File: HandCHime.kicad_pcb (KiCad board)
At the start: 4 copper layers, 38.1 x 22.6 mm, 18 parts, among them J1 USB_C_Receptacle_USB2.0, J2 Pins, SW0 BOOT, SW1 Row 0, Col 0, SW2 Row 0, Col 1, U1 CH552T, U2 USBLC6-2P6

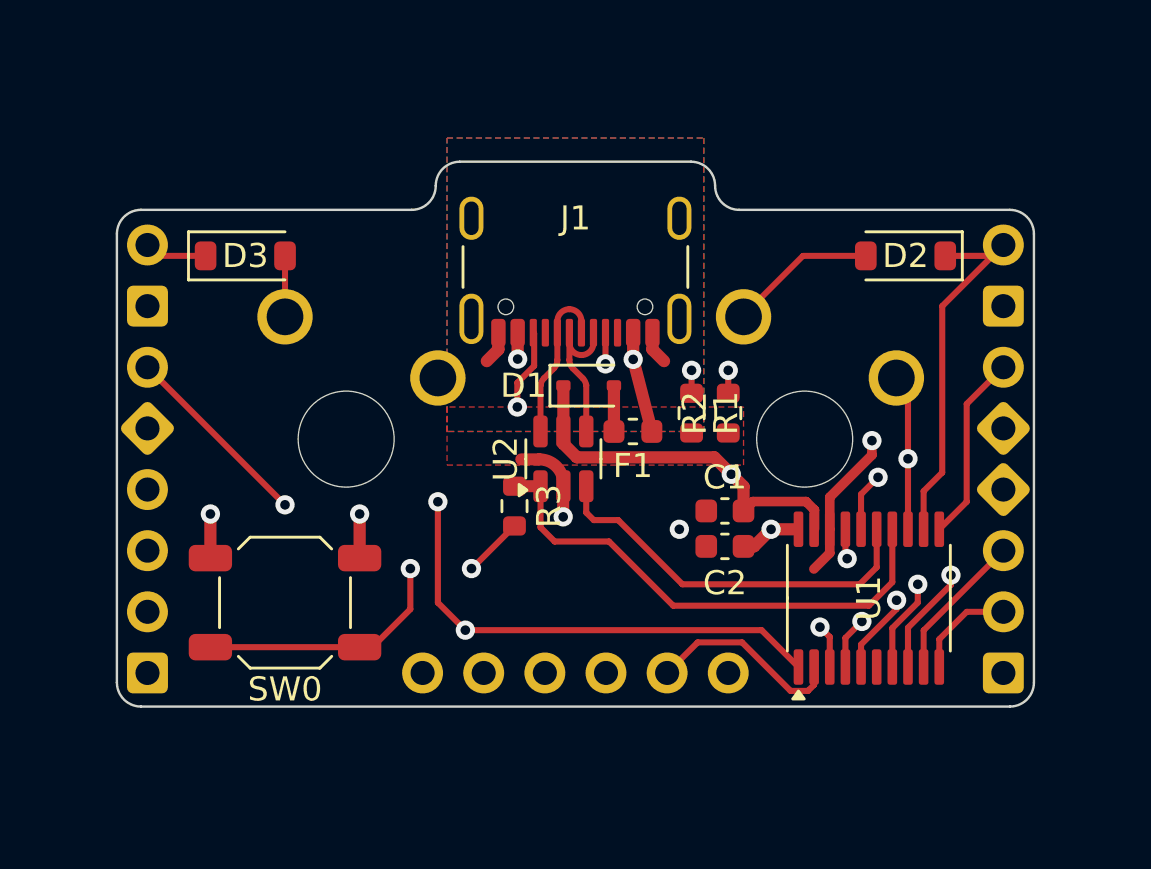
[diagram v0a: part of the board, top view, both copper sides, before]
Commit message: Try moving MCU to central part of board
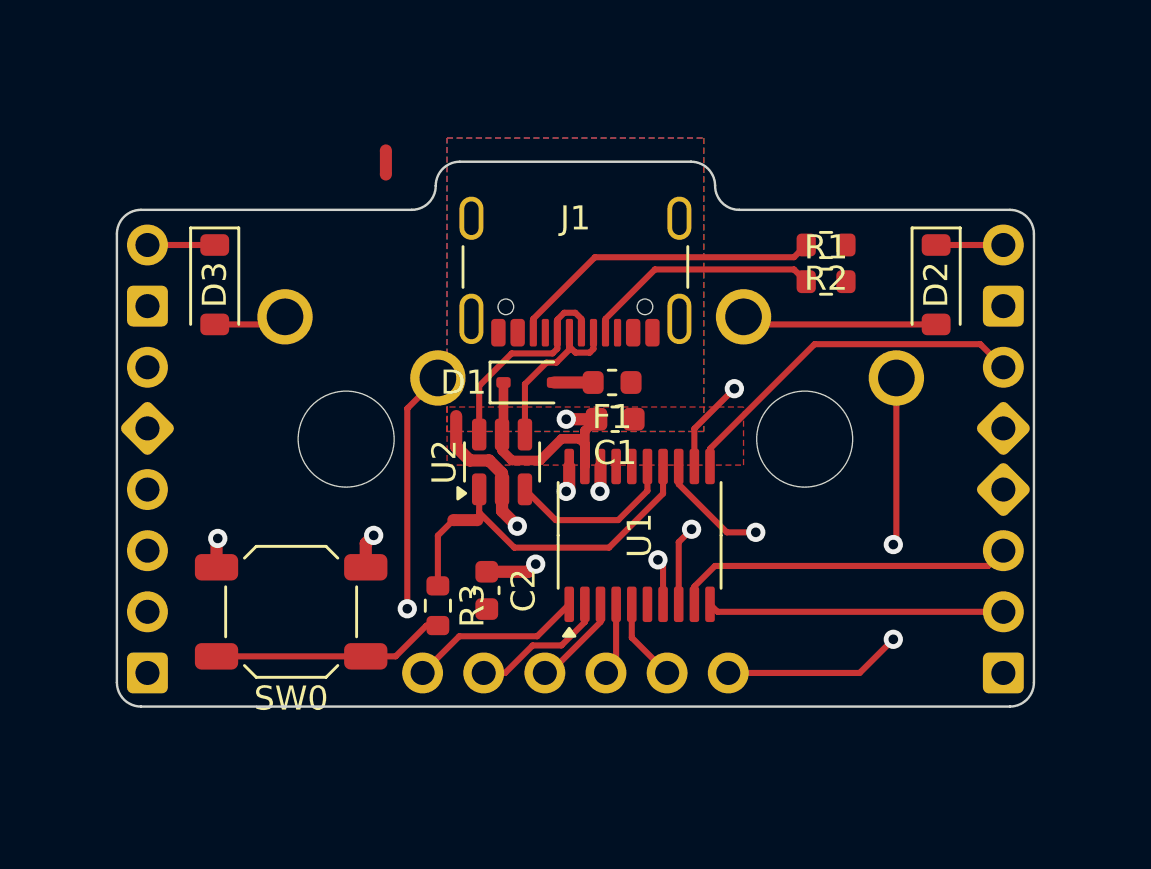
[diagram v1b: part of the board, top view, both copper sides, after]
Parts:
- moved NT1 16.0 mm to (150.9, 37.7)
- moved C2 10.1 mm to (155.1, 55.5), turned to -90 degrees
- moved U1 9.88 mm to (161.4, 53.2)
- moved R2 8.08 mm to (169.2, 41.1), turned to 0 degrees
- moved R1 7.81 mm to (169.2, 42.7), turned to 0 degrees
- moved C1 5.94 mm to (160.4, 48.4), turned to 0 degrees
- moved R3 5.22 mm to (153.0, 56.1)
- moved NT2 2.90 mm to (154.2, 52.6)
- moved U2 2.55 mm to (155.7, 50.2)
- moved D1 2.49 mm to (156.8, 46.9)
- moved F1 2.21 mm to (160.3, 46.9)
- moved D2 1.75 mm to (173.7, 42.8), turned to -90 degrees
- moved D3 1.75 mm to (143.8, 42.8), turned to -90 degrees
- moved SW0 0.46 mm to (146.9, 56.4)
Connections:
- J2 pad 10: P17 -> P14
- J2 pad 11: P16 -> P15
- J2 pad 12: P15 -> P16
- J2 pad 13: P14 -> P17
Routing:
- net P13: track 37.2 -> 0.00 mm, vias 2 -> 0
- net P12: track 32.5 -> 0.00 mm, vias 1 -> 0
- net P17: track 21.8 -> 3.46 mm, vias 1 -> 0
- net P16: track 16.6 -> 3.03 mm, vias 1 -> 0
- net P10: track 37.2 -> 24.0 mm
- net P11: track 39.5 -> 27.0 mm
- net VBUS: track 11.3 -> 0.00 mm, vias 2 -> 0
- net UDM: track 16.3 -> 7.14 mm
- net UDP: track 20.3 -> 11.3 mm
- net TX: track 4.29 -> 12.3 mm
- net RX: track 6.41 -> 14.2 mm
- net C1: track 27.9 -> 20.3 mm, vias 2 -> 1
- net P15: track 11.5 -> 3.93 mm, vias 1 -> 0
- net P33: track 7.83 -> 15.1 mm
- net Net-(R3-Pad2): track 15.7 -> 9.73 mm, vias 2 -> 0
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
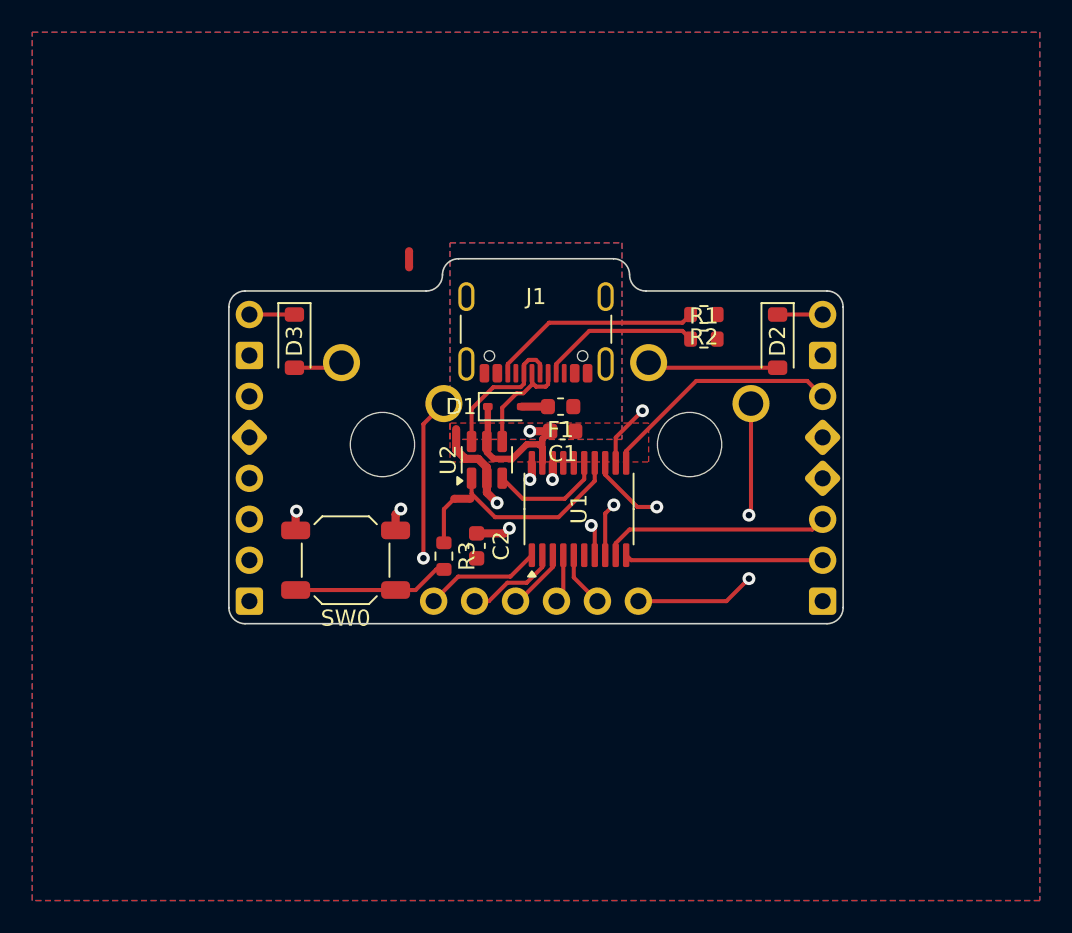
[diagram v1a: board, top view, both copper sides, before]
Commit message: Move MCU to centre of board and reroute
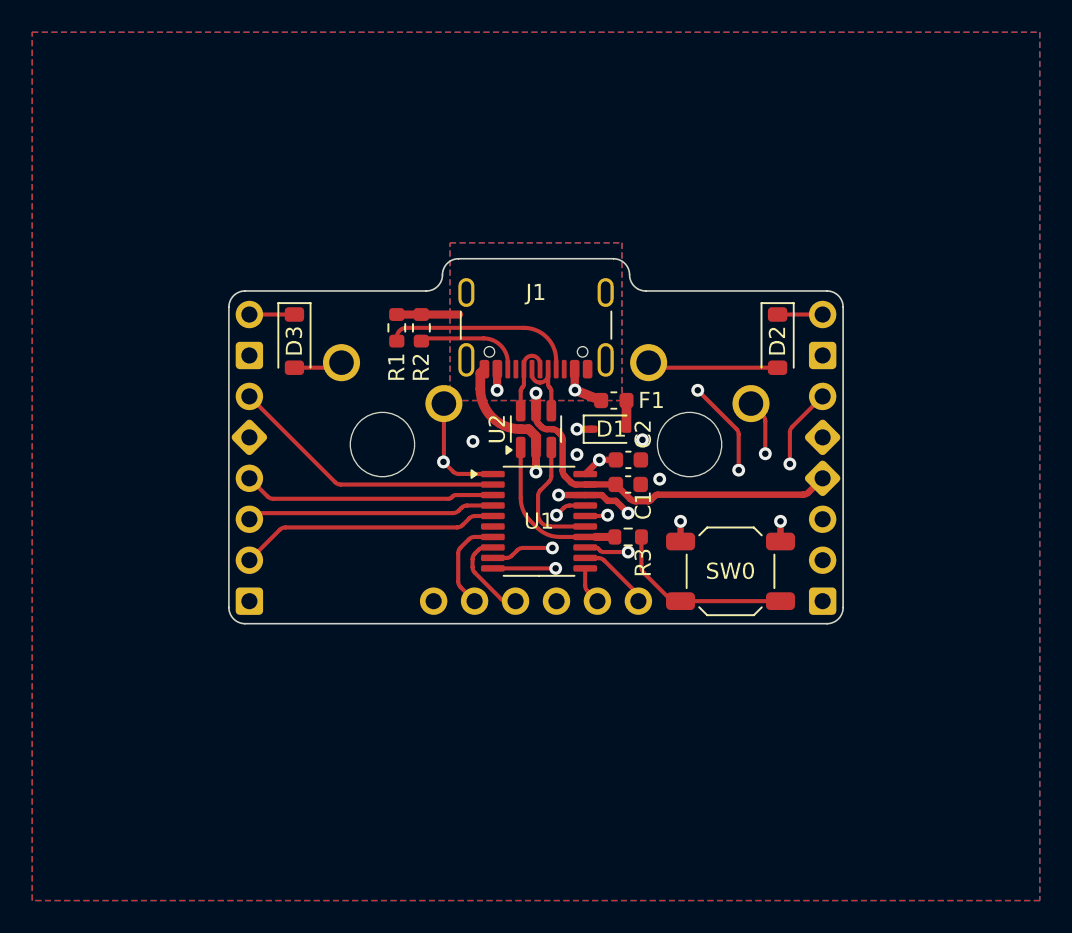
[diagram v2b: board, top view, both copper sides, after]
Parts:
- moved SW0 23.9 mm to (170.8, 57.1)
- moved R1 19.1 mm to (150.1, 42.0), turned to 90 degrees
- moved R2 17.5 mm to (151.6, 42.0), turned to 90 degrees
- moved NT1 14.9 mm to (158.8, 50.4)
- moved R3 11.5 mm to (164.5, 54.9), turned to 0 degrees
- moved C2 10.8 mm to (164.5, 50.2), turned to 0 degrees
- moved NT2 9.08 mm to (162.9, 54.9), turned to 180 degrees
- moved D1 6.65 mm to (163.3, 48.3)
- moved C1 5.24 mm to (164.5, 51.7)
- moved U2 3.60 mm to (158.8, 48.3)
- moved F1 3.32 mm to (163.6, 46.5), turned to 0 degrees
- moved U1 2.59 mm to (158.9, 54.0), turned to 0 degrees
- moved J1 0.25 mm to (158.8, 40.9)
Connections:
- net P_DM renamed USB_C-
- net P_DP renamed USB_C+
- net UDM renamed USB-
- net UDP renamed USB+
- J2 pad 10: P14 -> P10
- J2 pad 11: P15 -> P11
- J2 pad 12: P16 -> P12
- J2 pad 13: P17 -> P33
- J2 pad 20: P33 -> P35
- J2 pad 3: P13 -> P14
- J2 pad 5: P12 -> P15
- J2 pad 6: P11 -> P16
- J2 pad 7: P10 -> P17
- U1 pad 12: R0 -> C0
- U1 pad 13: C0 -> P35
- U1 pad 16: P13 -> R0
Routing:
- net P11: track 27.0 -> 4.66 mm, vias 1 -> 0
- net P35: track 0.00 -> 20.5 mm, vias 0 -> 2
- net P10: track 24.0 -> 6.01 mm, vias 1 -> 0
- net P33: track 15.1 -> 2.32 mm
- net P17: track 3.46 -> 16.2 mm
- net P15: track 3.93 -> 15.7 mm
- net P16: track 3.03 -> 14.7 mm
- net P14: track 5.82 -> 17.3 mm
- net VBUS: track 0.00 -> 9.80 mm, vias 0 -> 2
- net P12: track 0.00 -> 9.72 mm, vias 0 -> 1
- net TX: track 12.3 -> 21.5 mm, vias 0 -> 1
- net RX: track 14.2 -> 22.5 mm, vias 0 -> 1
- net Net-(J1-CC2): track 13.2 -> 5.83 mm
- net GND: track 1.04 -> 6.79 mm, vias 1 -> 7
- net USB_C+: track 8.91 -> 4.17 mm
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
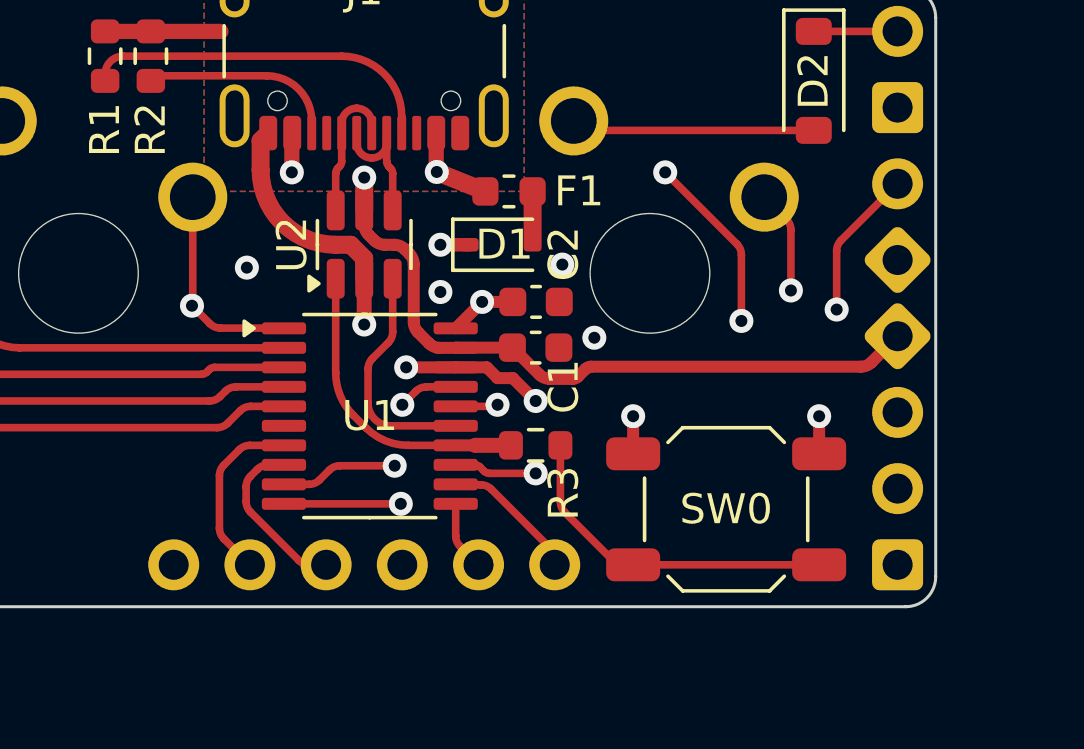
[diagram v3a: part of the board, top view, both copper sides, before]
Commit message: Straighten VCC track from MCU to pin
Other routing tweaks
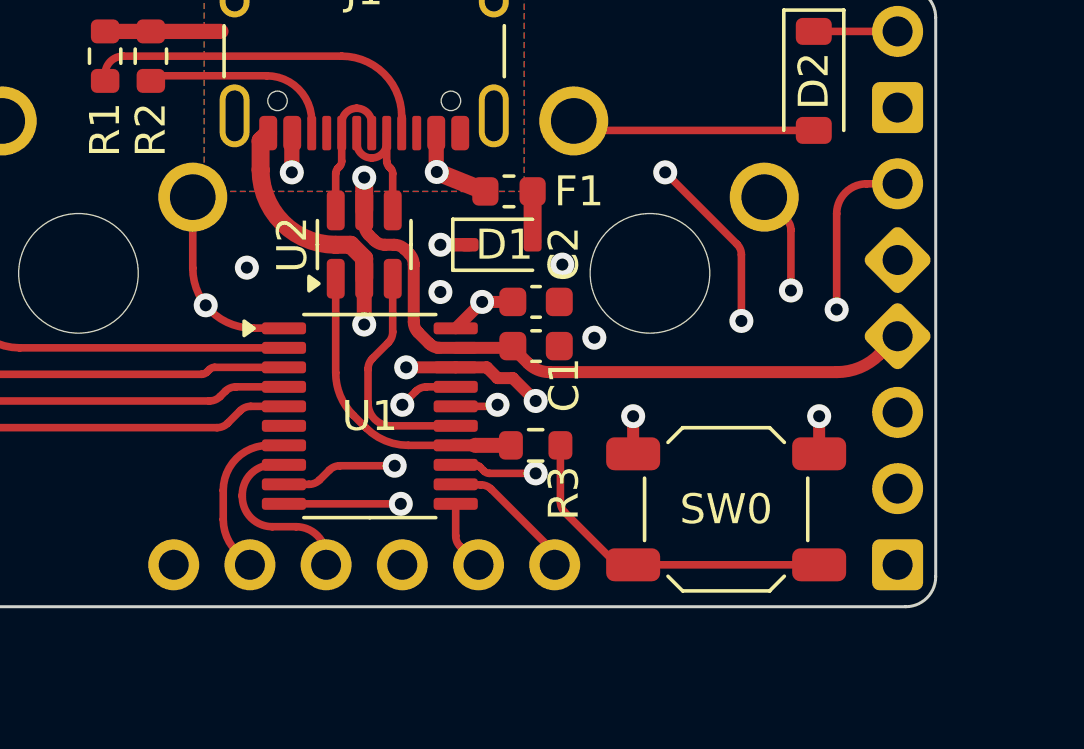
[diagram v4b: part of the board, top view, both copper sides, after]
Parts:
- moved C1 0.05 mm to (164.5, 51.6)
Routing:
- net P11: track 4.66 -> 6.11 mm
- net P35: track 20.5 -> 21.3 mm

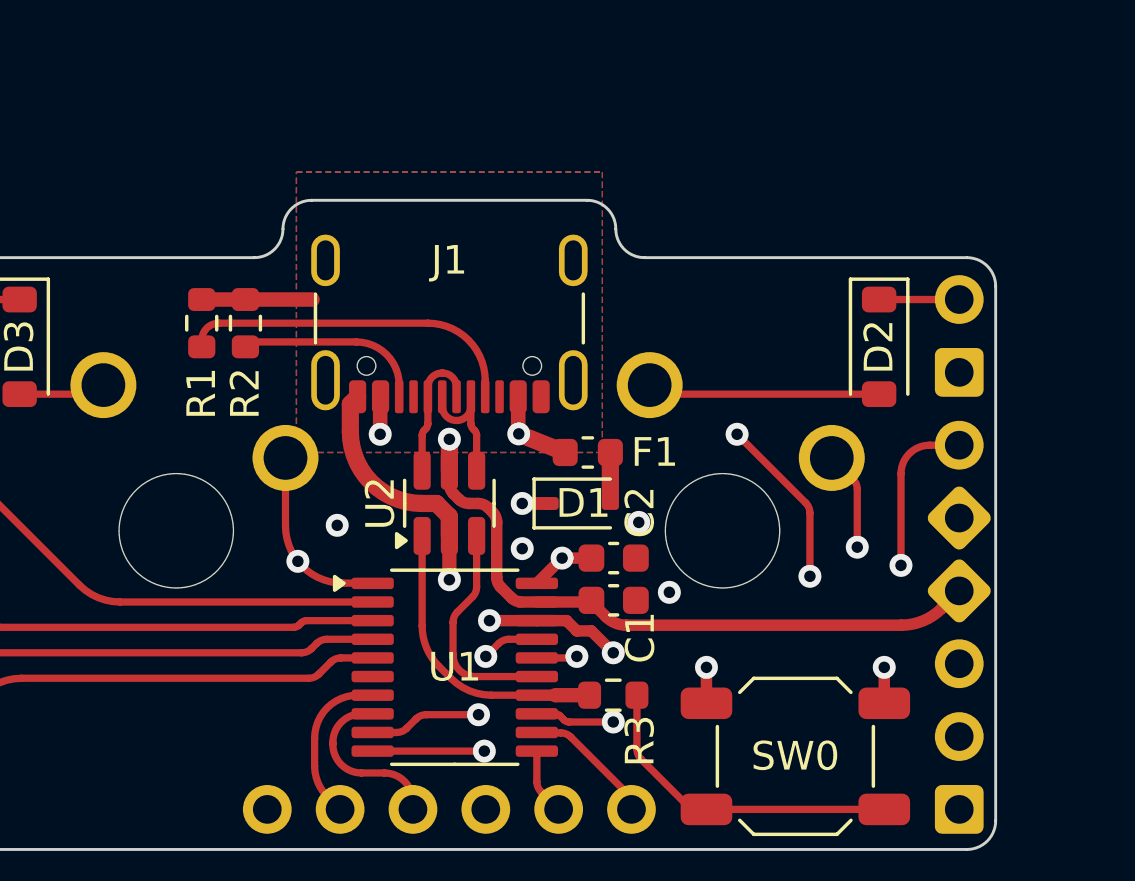
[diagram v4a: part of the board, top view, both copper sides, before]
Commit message: Use trace for 3V3, other routing tweaks
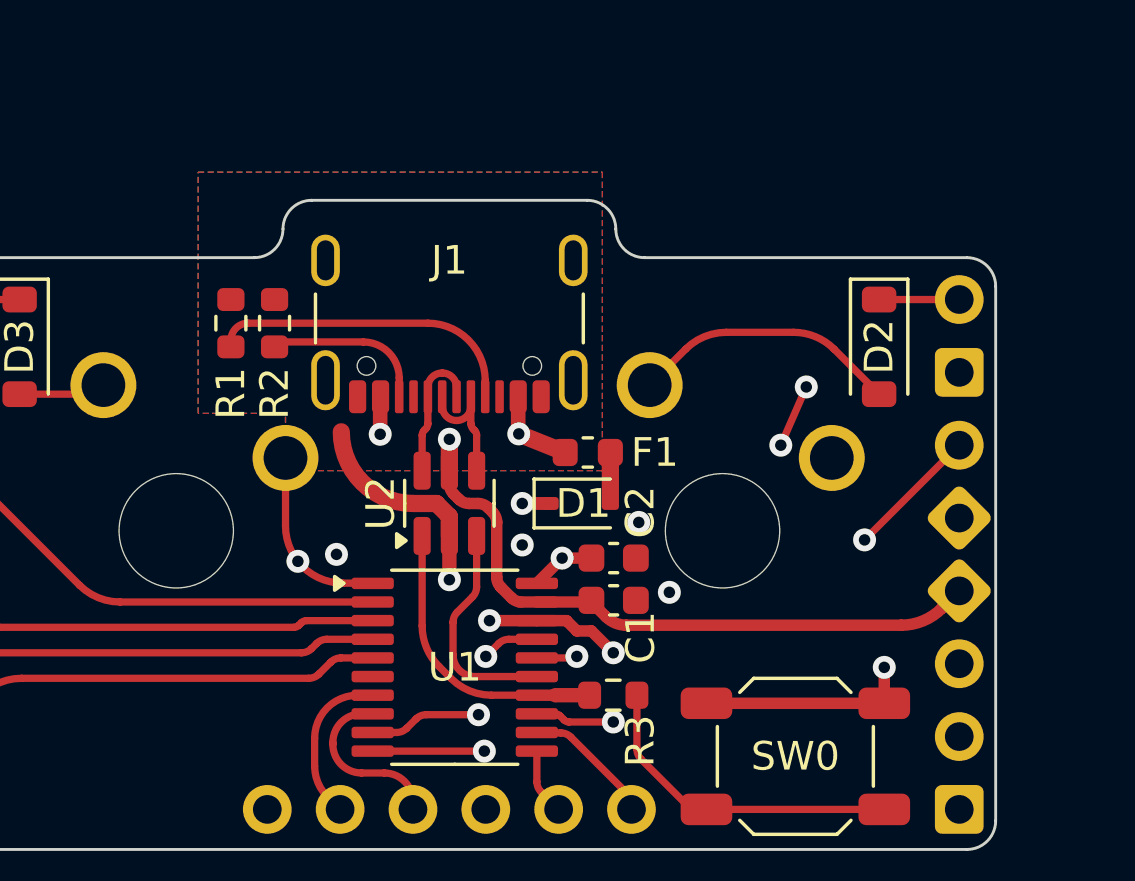
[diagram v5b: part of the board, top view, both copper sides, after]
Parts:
- moved R1 1.02 mm to (151.1, 42.0)
- moved R2 1.02 mm to (152.7, 42.0)
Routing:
- net +3V3: track 4.41 -> 58.2 mm, vias 3 -> 2
- net GNDPWR: track 10.8 -> 5.96 mm
- net Net-(D2-A): track 7.69 -> 9.46 mm
- net R0: track 64.0 -> 65.3 mm
- net Net-(J1-CC1): track 11.8 -> 10.8 mm
- net C0: track 34.1 -> 33.5 mm, vias 1 -> 0
- removed copper zone on In2.Cu, net +3V3
